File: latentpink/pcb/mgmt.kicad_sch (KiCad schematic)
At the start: 0 parts

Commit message: Continued initial schematic capture and floorplanning
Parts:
- added U4: STM32H735-UFBGA176-25, azonenberg_pcb:BGA_201_10x10_DEPOP_0.65MM_OSHPARK, symbol st-azonenberg:STM32H735-UFBGA176-25
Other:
- company: (none) -> Antikernel Labs

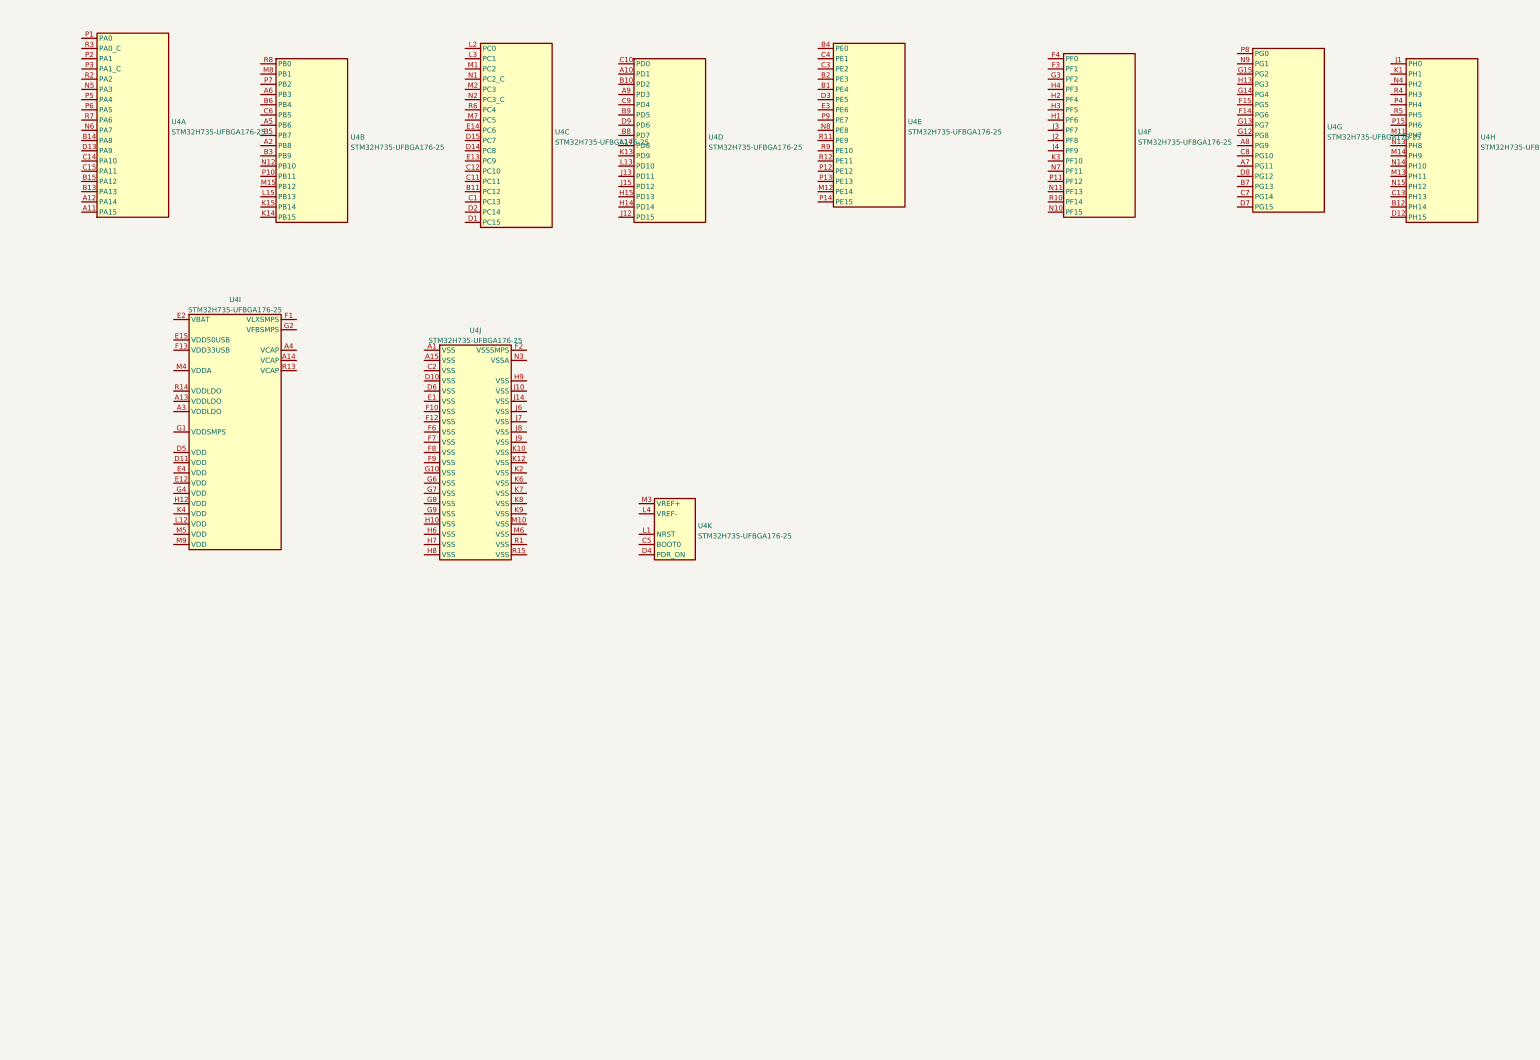
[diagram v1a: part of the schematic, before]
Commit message: Continued initial schematic capture
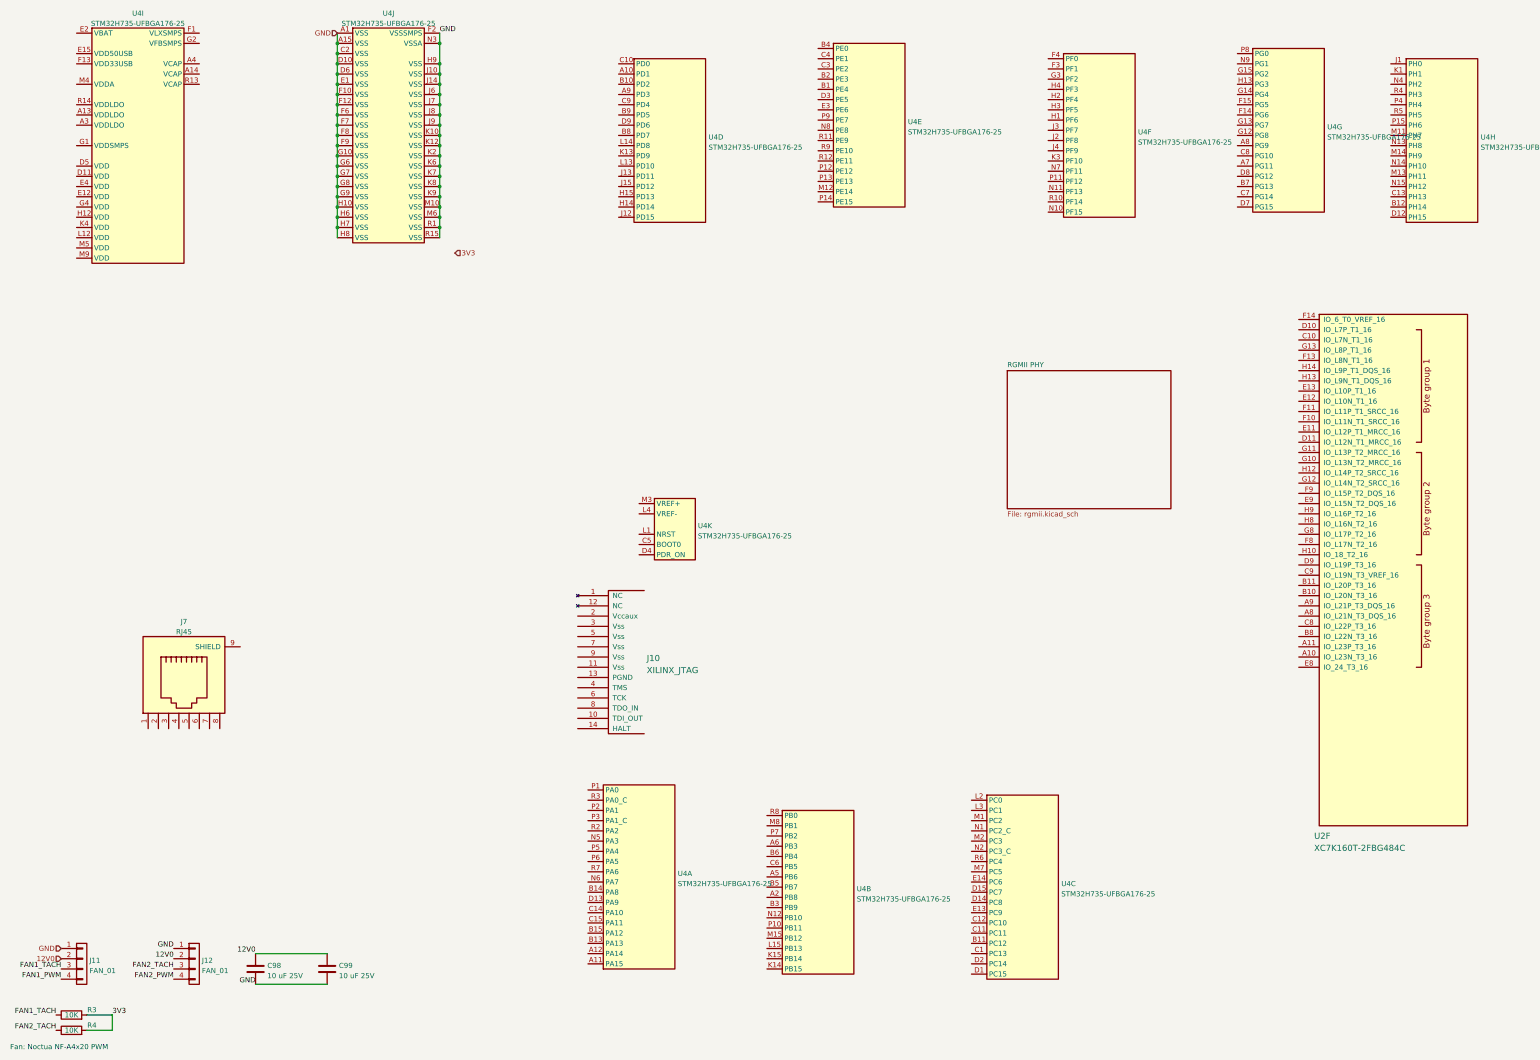
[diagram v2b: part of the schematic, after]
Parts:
- added C98, C99: 10 uF 25V, symbol device:C
- added J10: XILINX_JTAG, azonenberg_pcb:XILINX_JTAG_PTH_MOLEX_0878311420, symbol xilinx-azonenberg:XILINX_JTAG
- added J11, J12: FAN_01, symbol conn:CONN_01X04
- added J7: RJ45, azonenberg_pcb:CONN_RJ45_BELSTEWART_SS-7188S-A-PG4-1-BA-xx, symbol conn:RJ45
- added R3, R4: 10K, azonenberg_pcb:EIA_0402_RES_NOSILK, symbol device:R
- added U2: XC7K160T-2FBG484C, azonenberg_pcb:BGA_484_22x22_FULLARRAY_1MM, symbol xilinx-azonenberg:XC7KxT-FBG484
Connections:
- net GND: now reaches U4.A1 (VSS)
- net GND: now also U4.A15 (VSS), U4.C2 (VSS), U4.D10 (VSS), U4.D6 (VSS), U4.E1 (VSS), U4.F10 (VSS), U4.F12 (VSS), U4.F2 (VSSSMPS), U4.F6 (VSS), U4.F7 (VSS), U4.F8 (VSS), U4.F9 (VSS), U4.G10 (VSS), U4.G6 (VSS), U4.G7 (VSS), U4.G8 (VSS), U4.G9 (VSS), U4.H10 (VSS), U4.H6 (VSS), U4.H7 (VSS), U4.H8 (VSS), U4.H9 (VSS), U4.J10 (VSS), U4.J14 (VSS), U4.J6 (VSS), U4.J7 (VSS), U4.J8 (VSS), U4.J9 (VSS), U4.K10 (VSS), U4.K12 (VSS), U4.K2 (VSS), U4.K6 (VSS), U4.K7 (VSS), U4.K8 (VSS), U4.K9 (VSS), U4.M10 (VSS), U4.M6 (VSS), U4.N3 (VSSA), U4.R1 (VSS), U4.R15 (VSS), C98.2, C99.2, J11.1 (P1), J12.1 (P1)
- new net 12V0: C98.1, C99.1, J11.2 (P2), J12.2 (P2)
- new net 3V3: R3.2, R4.2
- new net FAN1_PWM: J11.4 (P4)
- new net FAN1_TACH: J11.3 (P3), R3.1
- new net FAN2_PWM: J12.4 (P4)
- new net FAN2_TACH: J12.3 (P3), R4.1
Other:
- added sheet RGMII PHY (rgmii.kicad_sch)
- note added: "Fan: Noctua NF-A4x20 PWM"
- moved on the sheet: U4A, U4B, U4C, U4I, U4J

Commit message: Initial version of RGMII PHY schematic
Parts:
- added C202, C203, C206, C208, C210: 4.7 uF, azonenberg_pcb:EIA_0603_CAP_NOSILK, symbol device:C
- added C204: 10 uF, azonenberg_pcb:EIA_0805_CAP_NOSILK, symbol device:C
- added C205, C209: 2.2 uF, azonenberg_pcb:EIA_0603_CAP_NOSILK, symbol device:C
- added C207, C226: 0.1 uF, azonenberg_pcb:EIA_0402_CAP_NOSILK, symbol device:C
- added C211, C212, C213, C215, C216, C219, C220, C222, C223, C224, C225, C227: 0.47 uF, azonenberg_pcb:EIA_0402_CAP_NOSILK, symbol device:C
- added C214: 22 uF, azonenberg_pcb:EIA_1206_CAP_NOSILK, symbol device:C
- added C217, C221: 10 uF, symbol device:C
- added C218: 220 pF, symbol device:C
- added FB5: FERRITE_SMALL2, azonenberg_pcb:EIA_0603_INDUCTOR_NOSILK, symbol passive-azonenberg:FERRITE_SMALL2
- added J15: CONN_01X03, symbol conn:CONN_01X03
- added L1: 2.2 uH, symbol passive-azonenberg:INDUCTOR_PWROUT
- added R48, R49: 10K, azonenberg_pcb:EIA_0402_RES_NOSILK, symbol device:R
- added R50: 33, symbol device:R
- added R51, R52: 4.7K, azonenberg_pcb:EIA_0402_RES_NOSILK, symbol device:R
- added TP17, TP18: U.FL, azonenberg_pcb:CONN_U.FL_TE_1909763-1, symbol conn:CONN_COAXIAL
- added U20: AT24MAC402, azonenberg_pcb:DFN_8_0.5MM_2x3MM_TALL, symbol memory-azonenberg:24Cxx-DFN8
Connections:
- net 3V3: now also J10.2 (Vccaux), U4.D11 (VDD), U4.D4 (PDR_ON), U4.D5 (VDD), U4.E12 (VDD), U4.E15 (VDD50USB), U4.E2 (VBAT), U4.E4 (VDD), U4.F13 (VDD33USB), U4.G1 (VDDSMPS), U4.G4 (VDD), U4.H12 (VDD), U4.K4 (VDD), U4.L12 (VDD), U4.M3 (VREF+), U4.M5 (VDD), U4.M9 (VDD), C202.1, C204.1, C206.1, C207.1, C208.1, C211.1, C212.2, C214.1, C215.1, C216.2, C219.1, C220.2, C222.1, C223.2, C224.1, C225.2, C227.1, FB5.1, J15.1 (P1), R49.1, R51.2, R52.2, U20.7 (WP_N), U20.8 (VDD)
- net GND: now also J10.11 (Vss), J10.3 (Vss), J10.5 (Vss), J10.7 (Vss), J10.9 (Vss), U4.L4 (VREF-), C202.2, C203.2, C204.2, C205.2, C206.2, C207.2, C208.2, C209.2, C210.2, C211.2, C212.1, C213.2, C214.2, C215.2, C216.1, C217.2, C218.2, C219.2, C220.1, C221.2, C222.2, C223.1, C224.2, C225.1, C226.2, C227.2, J15.3 (P3), TP17.2 (Ext), TP18.2 (Ext), U20.1 (A0), U20.2 (A1), U20.3 (A2), U20.4 (VSS)
- net MCU_BOOT0: now reaches U4.C5 (BOOT0)
- net MCU_BOOT0: now also R48.1
- net MCU_RST_N: now reaches U4.L1 (NRST)
- net MCU_RST_N: now also C226.1
- net MCU_QSPI_DQ3: now reaches U2.A10 (IO_L23N_T3_16)
- net MCU_QSPI_DQ3: now also U4.P2 (PA1)
- net MCU_QSPI_DQ2: now reaches U2.A11 (IO_L23P_T3_16)
- net MCU_QSPI_DQ2: now also U4.M1 (PC2)
- net MCU_QSPI_CLK: now reaches U2.A8 (IO_L21N_T3_DQS_16)
- net MCU_QSPI_CLK: now also U4.P7 (PB2)
- net MCU_IRQ: now reaches U2.A9 (IO_L21P_T3_DQS_16)
- net MCU_IRQ: now also U4.P1 (PA0)
- net MCU_QSPI_DQ1: now reaches U2.B8 (IO_L22N_T3_16)
- net MCU_QSPI_DQ1: now also U4.R8 (PB0)
- net MCU_QSPI_DQ0: now reaches U2.C8 (IO_L22P_T3_16)
- net MCU_QSPI_DQ0: now also U4.R2 (PA2)
- net ETH_LED2_P: now reaches U2.D10 (IO_L7P_T1_16)
- net MCU_QSPI_CS_N: now reaches U2.E8 (IO_24_T3_16)
- net MCU_QSPI_CS_N: now also U4.R12 (PE11)
- net ETH_LED1_P: now reaches U2.F14 (IO_6_T0_VREF_16)
- net MCU_JTAG_TDI: now reaches J10.10 (TDI_OUT)
- net MCU_JTAG_TDI: now also U4.A11 (PA15)
- net MCU_JTAG_TMS: now reaches J10.4 (TMS)
- net MCU_JTAG_TMS: now also U4.B13 (PA13)
- net MCU_JTAG_TCK: now reaches J10.6 (TCK)
- net MCU_JTAG_TCK: now also U4.A12 (PA14)
- net MCU_JTAG_TDO: now reaches J10.8 (TDO_IN)
- net MCU_JTAG_TDO: now also R50.1
- net MCU_VSMPS: now reaches U4.A13 (VDDLDO)
- net MCU_VSMPS: now also U4.A3 (VDDLDO), U4.R14 (VDDLDO)
- net VCORE: now reaches U4.A14 (VCAP)
- net VCORE: now also U4.A4 (VCAP), U4.R13 (VCAP), C205.1, C209.1, TP17.1 (In)
- net VLXSMPS: now reaches U4.F1 (VLXSMPS)
- net VLXSMPS: now also C218.1, L1.2
- net VSMPS: now reaches U4.G2 (VFBSMPS)
- net VSMPS: now also C203.1, C217.1, C221.1, L1.1, TP18.1 (In)
- net MCU_VDDA: now reaches U4.M4 (VDDA)
- net MCU_UART_TX: now reaches U4.B15 (PA12)
- net MCU_UART_RX: now reaches U4.C15 (PA11)
- net at U4.A6 (PB3): now also R50.2
- new net: J15.2 (P2), R48.2
- new net I2C_SCL: R51.1, U20.6 (SCL)
- new net I2C_SDA: R52.1, U20.5 (SDA)
- new net TRST: R49.2
- new net VDDA: C210.1, C213.1, FB5.2
- no-connect marks 0 -> 2
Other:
- sheet RGMII PHY ports: added 1V2, 1V8_IO, 2V5, 3V3, ETH_LED1_P, ETH_LED2_P, GND; removed none
- note added: "MCU VBAT decoupling"
- note added: "MCU VCAP decoupling"
- note added: "MCU VDD decoupling"
- note added: "MCU VDDA decoupling"
- note added: "MCU VDDLDO decoupling"
- note added: "MCU VDDSMPS decoupling"
- moved on the sheet: J10, J7, U4A, U4B, U4C, U4D, U4E, U4F, U4G, U4H, U4J, U4K

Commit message: Continued work on QSGMII subsystem
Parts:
- removed unit 8 of U4
- added C257: 0.47 uF, azonenberg_pcb:EIA_0402_CAP_NOSILK, symbol device:C
- added C258, C259, C260, C261: 0.1 uF, azonenberg_pcb:EIA_0402_CAP_NOSILK, symbol device:C
- added J16, J17: JUMPER_0402_SPDT, azonenberg_pcb:EIA_0402_JUMPER, symbol special-azonenberg:JUMPER_0402_SPDT
- added R77: 10K, azonenberg_pcb:EIA_0402_RES_NOSILK, symbol device:R
- added U23: ADM3101E_QFN, symbol special-azonenberg:ADM3101E_QFN
- R50: footprint (none) -> azonenberg_pcb:EIA_0402_RES_NOSILK
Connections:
- net 3V3: now also C257.1, R77.1, U23.5 (VCC)
- net FAN1_PWM: now also U4.D3 (PE5)
- net FAN1_TACH: now also U2.C10 (IO_L7N_T1_16)
- net FAN2_PWM: now also U4.E3 (PE6)
- net FAN2_TACH: now also U2.G13 (IO_L8P_T1_16)
- net GND: now also J7.4, J7.5, J7.9 (SHIELD), C257.2, C259.2, C261.2, U23.6 (GND), U23.PAD (GND)
- net MCU_UART_RX: now also U23.2 (Rout)
- net MCU_UART_TX: now also U23.3 (Tin)
- net FPGA_SYSCLK_N: now reaches U2.D11 (IO_L12N_T1_MRCC_16)
- net FPGA_SYSCLK_P: now reaches U2.E11 (IO_L12P_T1_MRCC_16)
- net MCU_JTAG_TRST: now reaches U4.B6 (PB4)
- net MCU_JTAG_TRST: now also R77.2
- net RS232_TX_RJ45: now reaches J7.3
- net RS232_TX_RJ45: now also J16.2
- net RS232_RX_RJ45: now reaches J7.6
- net RS232_RX_RJ45: now also J17.2
- new net: C260.1, U23.1 (C1+)
- new net: C260.2, U23.12 (C1-)
- new net: C259.1, U23.7 (V-)
- new net: C258.1, U23.11 (C2+)
- new net: C258.2, U23.10 (C2-)
- new net: C261.1, U23.4 (V+)
- new net RS232_RX: J16.3, J17.1, U23.9 (Rin)
- new net RS232_TX: J16.1, J17.3, U23.8 (Tout)
- no-connect marks 2 -> 128
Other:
- note added: "Fan PWM signal Vil 0.8V so 3.3V / 5V output should be OK (per Intel spec, Noctua doesn't specify) Has pullup to 5V inside fan, so must be 5V tolerant pin"
- note added: "TODO: general purpose oscillator"
- note added: "TX/RX crossover jumpers in case we got the RJ45 pinout wrong :)"
- moved on the sheet: J7

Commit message: Switched to new RJ45 for LATENTPINK, continued general PHY schematic
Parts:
- J15: footprint (none) -> azonenberg_pcb:CONN_HEADER_2.54MM_1x3
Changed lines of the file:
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@@
   (paper "A3")
   (title_block
-    (date "2023-05-14")
+    (date "2023-05-15")
     (rev "0.1")
     (company "Antikernel Labs")
@@
       (effects (font (size 1.27 1.27)) (justify left))
     )
-    (property "Footprint" "" (id 2) (at 52.07 194.31 0)
-      (effects (font (size 1.27 1.27)) hide)
-    )
+    (property "Footprint" "azonenberg_pcb:CONN_HEADER_2.54MM_1x3" (id 2) (at 52.07 194.31 0)
+      (effects (font (size 1.27 1.27)) hide)
+    )

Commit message: Rearranged ports, added center tap capacitors
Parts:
- U23: footprint (none) -> azonenberg_pcb:QFN_12_0.5MM_3x3MM
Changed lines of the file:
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@@
     (property "Reference" "U23" (id 0) (at 147.32 197.011 0))
     (property "Value" "ADM3101E_QFN" (id 1) (at 147.32 199.5479 0))
-    (property "Footprint" "" (id 2) (at 140.97 231.14 0)
+    (property "Footprint" "azonenberg_pcb:QFN_12_0.5MM_3x3MM" (id 2) (at 140.97 231.14 0)
       (effects (font (size 1.27 1.27)) hide)
     )

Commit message: Continued initial component placement
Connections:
- net VDDA is gone; now on net MCU_VDDA: C210.1, C213.1, FB5.2
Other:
- sheet RGMII PHY ports: added CHGND; removed none
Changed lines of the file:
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@@
     (effects (font (size 1.27 1.27)) (justify right bottom))
   )
-  (label "VDDA" (at 63.5 110.49 0)
+  (label "MCU_VDDA" (at 63.5 110.49 0)
     (effects (font (size 1.27 1.27)) (justify left bottom))
   )
@@
     (effects (font (size 1.27 1.27)) (justify right bottom))
   )
-  (label "ETH_LED1_P" (at 314.96 219.71 180)
+  (label "ETH_LED1_P" (at 314.96 222.25 180)
     (effects (font (size 1.27 1.27)) (justify right bottom))
   )
@@
     (effects (font (size 1.27 1.27)) (justify right bottom))
   )
-  (label "ETH_LED2_P" (at 314.96 222.25 180)
+  (label "ETH_LED2_P" (at 314.96 224.79 180)
     (effects (font (size 1.27 1.27)) (justify right bottom))
   )
@@
     (effects (font (size 1.27 1.27)) (justify right))
   )
+  (hierarchical_label "CHGND" (shape input) (at 314.96 217.17 180)
+    (effects (font (size 1.27 1.27)) (justify right))
+  )
   (hierarchical_label "1V8_IO" (shape input) (at 314.96 209.55 180)
     (effects (font (size 1.27 1.27)) (justify right))
@@
     (pin "9")
   )
-  (sheet (at 314.96 201.93) (size 15.24 22.86) (fields_autoplaced)
+  (sheet (at 314.96 201.93) (size 15.24 25.4) (fields_autoplaced)
     (stroke (width 0.1524) (type solid) (color 0 0 0 0))
     (fill (color 0 0 0 0.0000))
@@
       (effects (font (size 1.27 1.27)) (justify left bottom))
     )
-    (property "Sheet file" "rgmii.kicad_sch" (id 1) (at 314.96 225.3746 0)
+    (property "Sheet file" "rgmii.kicad_sch" (id 1) (at 314.96 227.9146 0)
       (effects (font (size 1.27 1.27)) (justify left top))
     )
@@
       (effects (font (size 1.27 1.27)) (justify left))
     )
-    (pin "ETH_LED1_P" input (at 314.96 219.71 180)
+    (pin "ETH_LED1_P" input (at 314.96 222.25 180)
       (effects (font (size 1.27 1.27)) (justify left))
     )
@@
       (effects (font (size 1.27 1.27)) (justify left))
     )
-    (pin "ETH_LED2_P" input (at 314.96 222.25 180)
+    (pin "ETH_LED2_P" input (at 314.96 224.79 180)
       (effects (font (size 1.27 1.27)) (justify left))
     )
@@
       (effects (font (size 1.27 1.27)) (justify left))
     )
+    (pin "CHGND" input (at 314.96 217.17 180)
+      (effects (font (size 1.27 1.27)) (justify left))
+    )
